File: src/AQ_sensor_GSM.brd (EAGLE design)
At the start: 110 x 64 mm, 84 parts, among them IC1 MIC29302WU, IC2 MCP73831/OT, J1 F-1X03-SIP-100-32, J2 SIM8060-6-1-14-00-A, J3 PJ-002BH, Q1 MMBT2222, Q2 MMBT2222, Q3 MMBT2222, U1 LM7805S/NOPB, U2 TEXAS_INSTRUMENTS_SN74HC125TE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, U3 TEXAS_INSTRUMENTS_LM1117IMP-3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, U4 EC200UCNAB-N05-SNNSA, X1 53048-08

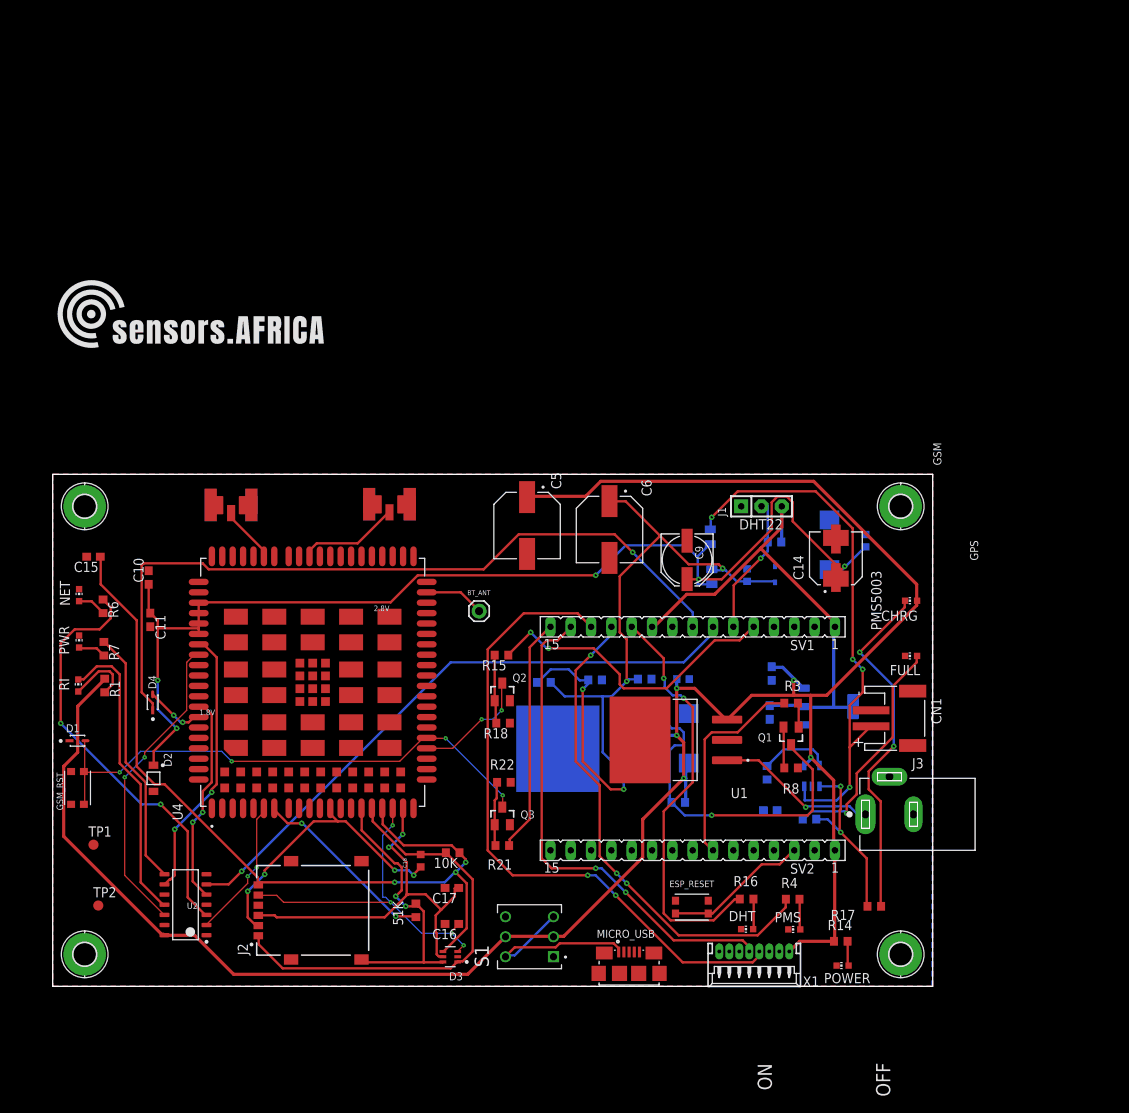
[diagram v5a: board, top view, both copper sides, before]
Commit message: Rearrange USB port and DC jack
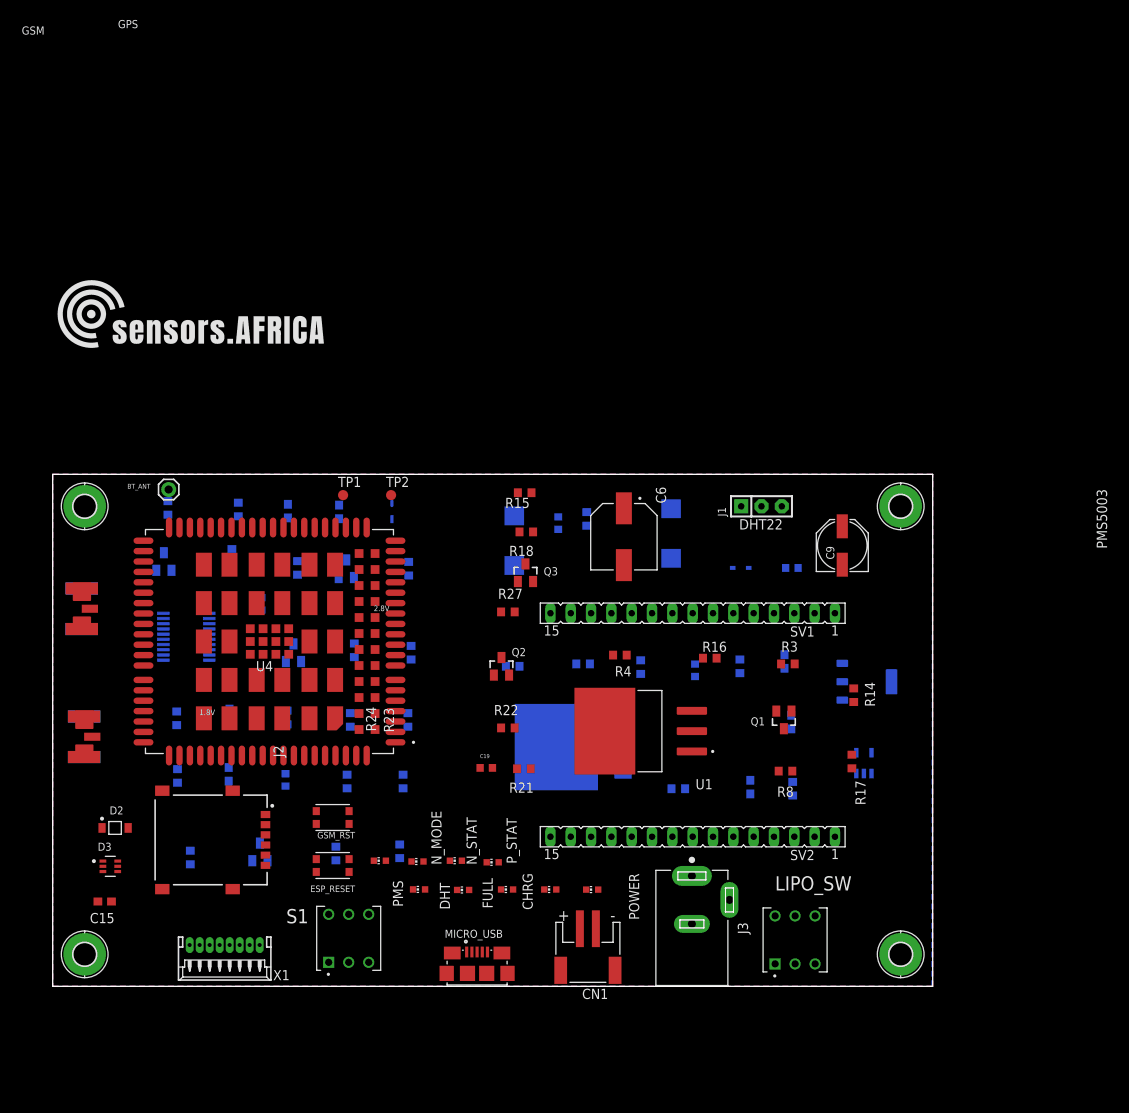
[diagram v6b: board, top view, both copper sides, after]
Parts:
- removed C14: EEEFT1E101AV, 100uf 25v capacitor:CAP_EEEFT1E101AV
- removed C5: EEEFN1C471P, EEEFN1C471P:CAP_EEEFN1C471P
- removed D4: ON_SEMI_1N4148WSON_SEMI_1N4148WS_0_0, AQ_sensor_GSM:ON_SEMI_1N4148WS_0
- removed NET: YELLOW, led:CHIP-LED0603
- removed PWR: RED, led:CHIP-LED0603
- removed R1, R6, R7: 470, rcl:R0603
- removed RI: ORANGE, led:CHIP-LED0603
- removed U2: TEXAS_INSTRUMENTS_SN74HC125TEXAS_INSTRUMENTS_SN74HC125_0_0, AQ_sensor_GSM:TEXAS_INSTRUMENTS_SN74HC125_0
- added C19, C20: 100nf, 06035C104K4T2A:CAPC1608X90N
- added LIPO_SW: TL2285EE, TL2285EE:SW_TL2285EE
- added M_RI, N_MODE, N_STAT, P_STAT: ORANGE, led:CHIP-LED0603
- added Q4, Q5, Q6, Q7: MMBT2222, MMBT2222_:SOT23-BEC
- added R23, R31, R34: 4.7K, rcl:R0603
- added R24, R32, R35: 47K, rcl:R0603
- added R25, R28, R33, R36: 470R, rcl:R0603
- added R26: 120K, rcl:R0603
- added R27: 10K, rcl:R0603
- added R29, R30: 51K, rcl:R0603
- added U5: TXS0108EPWR, TXS0108EPWR:SOP65P640X120-20N
- R12: value 0R -> 4.7K; device CR0805AJ_-000EAS:RESC2012X60N -> rcl:R0603
- R13: value 100M -> 47K; device CR0805AJ_-000EAS:RESC2012X60N -> rcl:R0603
- moved X1 66.2 mm to (21.5, 3.91)
- moved TP2 63.0 mm to (42.3, 61.4)
- moved FULL 58.3 mm to (56.8, 12.1)
- moved CHRG 57.8 mm to (62.2, 12.1)
- moved TP1 53.7 mm to (36.3, 61.4)
- moved CN1 49.3 mm to (66.9, 3.50), turned to 180 degrees
- moved D1 48.7 mm to (42.4, 59.4), flipped to the bottom, turned to 90 degrees
- moved PMS 47.2 mm to (45.8, 12.1)
- moved ESP_RESET 45.2 mm to (35.0, 15.1), turned to 180 degrees
- moved D3 44.0 mm to (7.20, 15.0), turned to 0 degrees
- moved GPS 43.2 mm to (1.60, 47.2), turned to 0 degrees
- moved C15 43.1 mm to (6.50, 10.6)
- moved BT_ANT 41.7 mm to (14.5, 62.1)
- moved R12 40.1 mm to (44.8, 41.7)
- moved C16 38.1 mm to (22.1, 33.8), flipped to the bottom, turned to 90 degrees
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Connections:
- removed net GSM_RX: D4.2, U4.68
- removed net GSM_RX_O: D4.1, SV1.8
- removed net GSM_TX: U2.5, U4.67
- removed net GSM_TX_5V: SV1.7, U2.6
- removed net N$10: NET.A, R6.2
- removed net N$11: PWR.A, R7.2
- removed net N$14: R1.2, RI.A
- removed net NETSTAT_5V: R6.1, U2.3
- removed net PWRSTAT_5V: R7.1, U2.8
- removed net RI: U2.12, U4.62
- removed net RI_5V: RI.C, U2.11
- new net BP: CN1.1, IC2.3, LIPO_SW.1, LIPO_SW.6
- new net CP: C6.1, C7.2, D5.C, IC1.4, LIPO_SW.2, LIPO_SW.5, R11.2, R9.2
- new net MAIN_CTS: U4.64, U5.4
- new net MAIN_DCD: U4.63, U5.3
- new net MAIN_DTR: U4.66, U5.6
- new net MAIN_RI: R34.1, U4.62, U5.1
- new net MAIN_RTS: U4.65, U5.5
- new net MAIN_RXD: U4.68, U5.8
- new net MAIN_TXD: U4.67, U5.7
- new net MCU_CTS: U5.17
- new net MCU_DCD: U5.18
- new net MCU_DTR: SV2.12, U5.15
- new net MCU_RI: U5.20
- new net MCU_RTS: U5.16
- new net MCU_RXD: SV1.8, U5.14
- new net MCU_TXD: SV1.7, U5.13
- new net N$26: Q4.B, R23.2, R24.2
- new net N$28: Q6.B, R31.2, R32.2
- new net N$29: Q4.C, R25.1
- new net N$30: N_MODE.C, R25.2
- new net N$31: R26.1, R27.2, U5.10
- new net N$32: Q6.C, R33.1
- new net N$40: R30.1, U5.9
- new net N$41: R29.1, U5.12
- new net N$42: Q7.B, R34.2, R35.2
- new net N$43: Q7.C, R36.1
- new net N$44: M_RI.C, R36.2
- new net NET_MODE: R23.1, U4.5
- net +3V3: now also C20.2, U5.19
- net +5V: no longer C5.1, R1.1, U2.14
- net GND: now also C19.1, C20.1, Q4.E, Q5.E, Q6.E, Q7.E, R13.1, R24.1, R26.2, R29.2, R30.2, R32.1, R35.1, U5.11; no longer C14.2, C5.2, NET.C, PWR.C, U2.1, U2.10, U2.13, U2.4, U2.7
- net N$22: now also Q5.B, R12.2, R13.2; no longer SV2.12
- net N$33: now also Q5.C, R28.1; no longer U4.66
- net N$34: now also N_STAT.C, R28.2; no longer C6.1, C7.2, D5.C, IC1.4, R11.2, R13.1, R9.2
- net N$39: now also P_STAT.C, R33.2; no longer CN1.1, IC2.3, R12.2
- net NETSTAT: now also R12.1; no longer U2.2
- net PWRSTAT: now also R31.1; no longer U2.9
- net VDD_EXT: now also C19.2, R27.1, U5.2
- net V_LIPO: now also LIPO_SW.3, LIPO_SW.4, M_RI.A, N_MODE.A, N_STAT.A, P_STAT.A; no longer C14.1, R12.1, R13.2
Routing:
- net +5V: track 286.1 -> 0.00 mm, vias 5 -> 0
- net V_LIPO: track 146.3 -> 0.00 mm, vias 5 -> 0
- net SIMDATA: track 103.5 -> 0.00 mm, vias 3 -> 0
- net GSM_RX_O: track 95.6 -> 0.00 mm, vias 1 -> 0
- net PMS_RX: track 81.2 -> 0.00 mm, vias 2 -> 0
- net GSM_TX_5V: track 77.1 -> 0.00 mm, vias 1 -> 0
- net N$34: track 69.9 -> 0.00 mm, vias 2 -> 0
- net N$39: track 67.9 -> 0.00 mm, vias 4 -> 0
- net PWRKEY: track 67.8 -> 0.00 mm, vias 4 -> 0
- net +3V3: track 63.1 -> 0.00 mm
- net PMS_TX: track 62.4 -> 0.00 mm, vias 2 -> 0
- net PMS_LED: track 61.6 -> 0.00 mm, vias 3 -> 0
- net USIM_VDD: track 56.7 -> 0.00 mm
- net NETSTAT_5V: track 53.3 -> 0.00 mm, vias 2 -> 0
- net DHT_LED: track 52.1 -> 0.00 mm, vias 2 -> 0
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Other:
- board text removed: "OFF"
- board text removed: "ON"

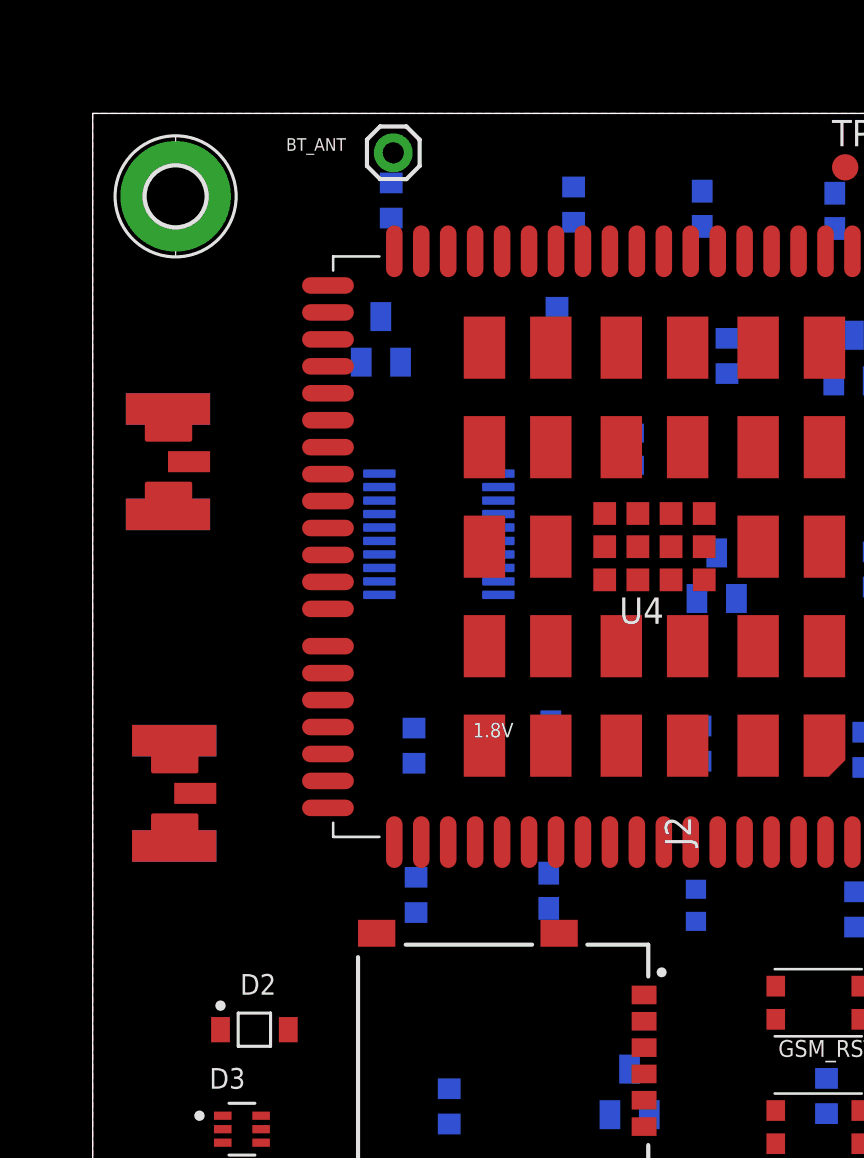
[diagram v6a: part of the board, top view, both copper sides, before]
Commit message: Added internal gsm Antenna
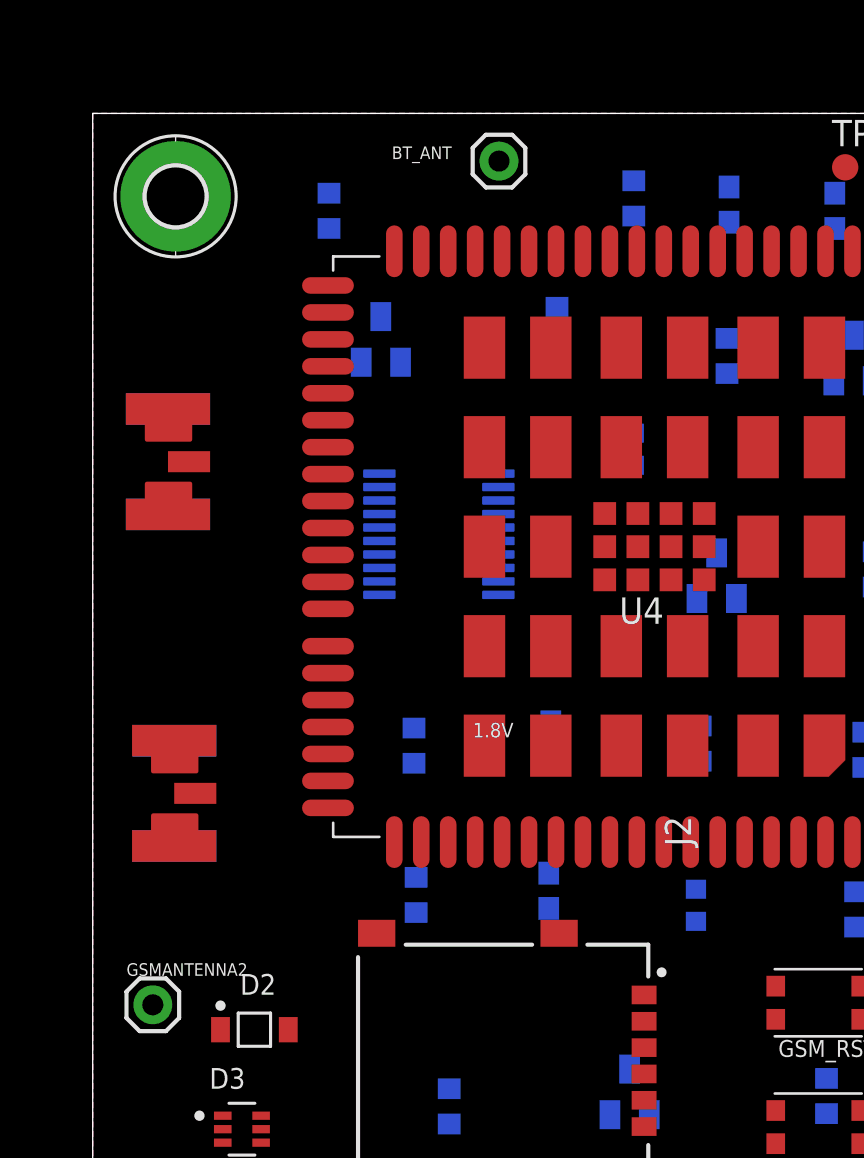
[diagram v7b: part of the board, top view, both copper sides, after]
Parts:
- added GSMANTENNA2: (no value), SparkFun-Connectors:1X01
- moved BT_ANT 5.12 mm to (19.6, 61.7)
- moved R36 3.04 mm to (11.4, 59.3)
- moved R34 2.92 mm to (26.1, 59.9), turned to 90 degrees
- moved C11 1.32 mm to (30.7, 59.6)
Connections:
- net GSM_ANT: now also GSMANTENNA2.1

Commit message: PCB Routed
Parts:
- moved ESP_RESET 70.6 mm to (105.5, 12.3)
- moved Q3 66.4 mm to (7.90, 9.40)
- moved R14 54.4 mm to (50.4, 58.5)
- moved N_STAT 48.0 mm to (2.50, 13.2)
- moved R17 44.2 mm to (55.9, 23.6), turned to 90 degrees
- moved N_MODE 43.0 mm to (2.60, 16.8)
- moved R19 40.2 mm to (52.3, 23.5), flipped to the top
- moved M_RI 38.6 mm to (2.80, 9.70)
- moved IC2 37.2 mm to (67.2, 13.3), flipped to the top
- moved R32 37.2 mm to (13.6, 39.1)
- moved U5 33.0 mm to (36.2, 17.1), flipped to the top, turned to 270 degrees
- moved R31 32.3 mm to (20.4, 45.2)
- moved Q6 31.0 mm to (13.9, 45.4)
- moved R15 29.7 mm to (86.8, 51.2)
- moved R20 29.5 mm to (72.3, 13.8), flipped to the top
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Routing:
- net V_LIPO: track 0.00 -> 281.3 mm, vias 0 -> 3
- net +3V3: track 0.00 -> 246.5 mm, vias 0 -> 2
- net +5V: track 0.00 -> 201.9 mm, vias 0 -> 7
- net CP: track 0.00 -> 165.8 mm, vias 0 -> 4
- net PWRKEY: track 0.00 -> 127.1 mm, vias 0 -> 2
- net SIMRST: track 0.00 -> 100.8 mm, vias 0 -> 4
- net N$34: track 0.00 -> 89.3 mm, vias 0 -> 1
- net USIM_DET: track 0.00 -> 85.4 mm, vias 0 -> 4
- net N$4: track 0.00 -> 85.2 mm, vias 0 -> 2
- net SIMCLK: track 0.00 -> 82.4 mm, vias 0 -> 4
- net N$2: track 0.00 -> 82.4 mm, vias 0 -> 2
- net SIMDATA: track 0.00 -> 78.0 mm, vias 0 -> 4
- net PMS_RX: track 0.00 -> 70.6 mm, vias 0 -> 3
- net BP: track 0.00 -> 69.6 mm
- net PMS_TX: track 0.00 -> 68.7 mm, vias 0 -> 3
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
